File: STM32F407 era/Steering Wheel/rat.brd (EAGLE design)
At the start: 99.2 x 116.2 mm, 103 parts, among them IC3 PCA82C250T, Q1 12 MHz

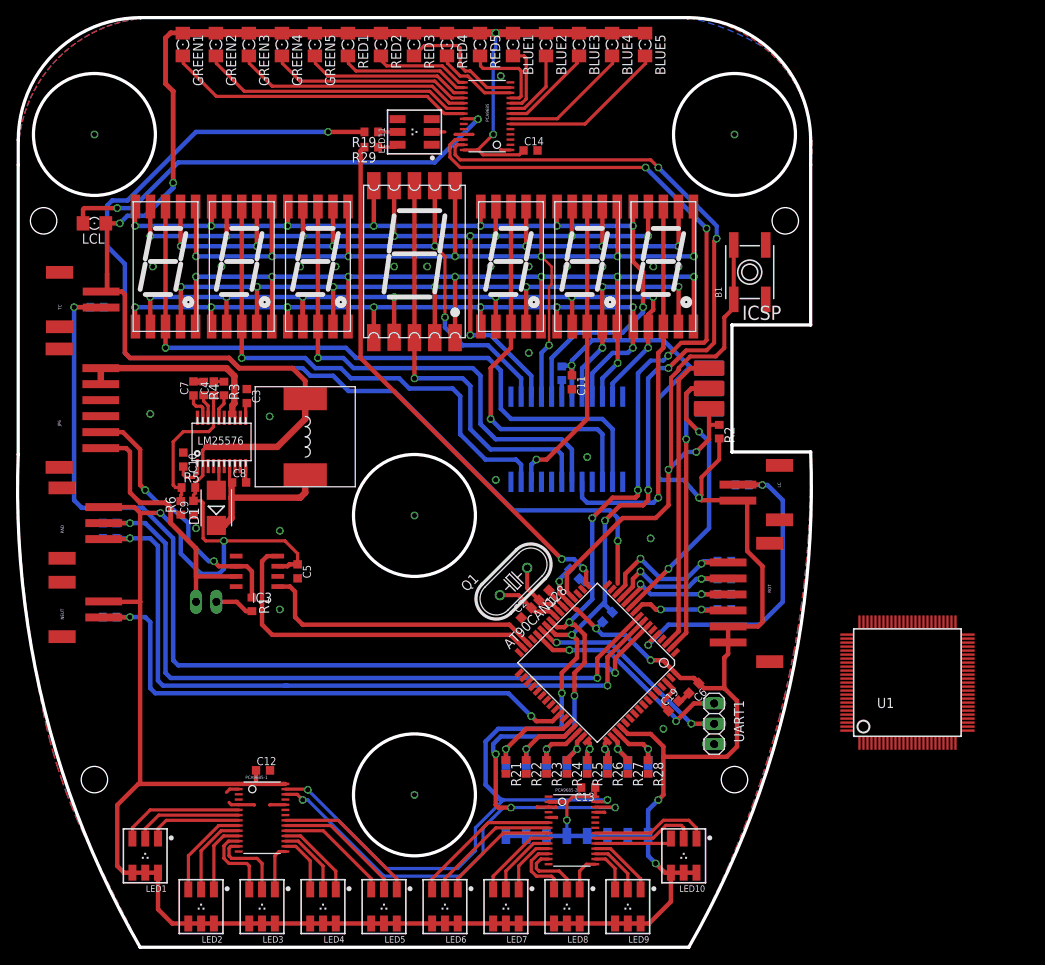
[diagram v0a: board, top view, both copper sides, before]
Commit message: added debounce handlers to critical buttons
Added MAX6817 debounce switches to the critical switches, and added the
acording datasheet
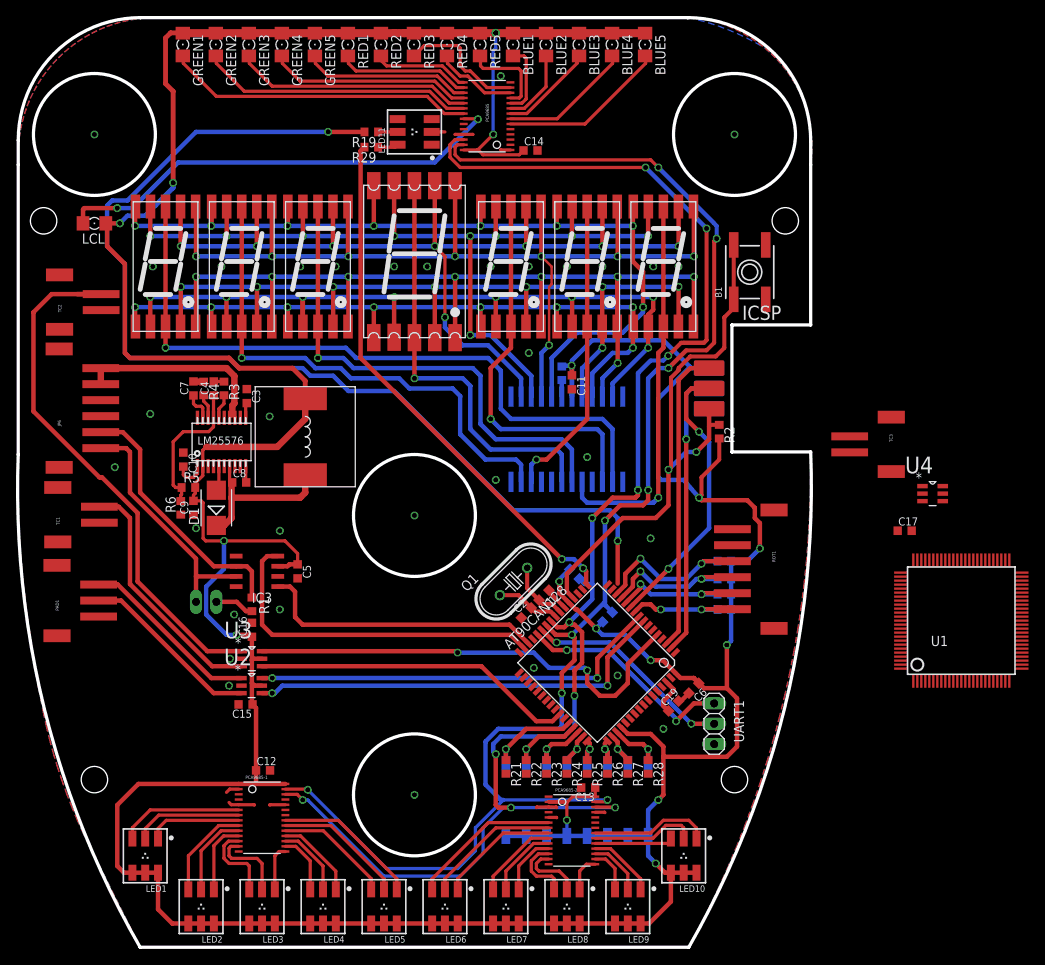
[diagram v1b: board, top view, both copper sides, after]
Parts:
- removed LC, NEUT, TC: (no value), unicorn_v2:S2B-PH
- removed PAD: (no value), unicorn_v2:S3B-PH
- removed R10, R12, R7, R8, R9: 10k, rcl:R0603
- removed ROT: M06, unicorn_v2:S6B_PH
- added C15, C16, C17: 100nF, rcl:C0603K
- added PAD1: (no value), unicorn_v2:S3B-PH
- added ROT1: M06, unicorn_v2:S6B_PH
- added TC1: NEUT, unicorn_v2:S2B-PH
- added TC2: LC, unicorn_v2:S2B-PH
- added TC3: tc, unicorn_v2:S2B-PH
- added U2, U3, U4: MAX6817EUT+T, Maxim_By_element14_Batch_1:SOT95P280X145-6N
- moved U1 10.3 mm to (290.0, 9.08)
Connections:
- new net N$85: TC1.2, U3.3
- new net N$86: PAD1.3, U2.1
- new net N$87: PAD1.2, U2.3
- new net N$88: TC2.2, U3.1
- new net N$90: TC3.2, U4.1
- net +5V: now also C15.1, C16.1, C17.1, R13.1, R14.1, R15.1, R16.1, U2.5, U3.5, U4.5; no longer LC.2, NEUT.2, PAD.3, ROT.5, ROT.6, TC.2
- net GND: now also C15.2, C16.2, C17.2, PAD1.1, ROT1.1, ROT1.2, TC1.1, TC2.1, TC3.1, U2.2, U3.2, U4.2; no longer R10.1, R12.1, R13.1, R14.1, R15.1, R16.1, R7.1, R8.1, R9.1
- net LC: now also U3.6; no longer LC.1, R9.2
- net NEUTRAL: now also U3.4; no longer NEUT.1, R8.2
- net PADDOWN: now also U2.4; no longer PAD.1, R10.2
- net PADUP: now also U2.6; no longer PAD.2, R12.2
- net ROTSW1: now also ROT1.6; no longer ROT.4
- net ROTSW2: now also ROT1.5; no longer ROT.3
- net ROTSW3: now also ROT1.4; no longer ROT.2
- net ROTSW4: now also ROT1.3; no longer ROT.1
- net TCTEMPOFF: now also U4.4; no longer R7.2, TC.1
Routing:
- net TCTEMPOFF: track 126.0 -> 0.00 mm, vias 2 -> 0
- net N$88: track 0.00 -> 68.3 mm
- net PADUP: track 90.8 -> 51.8 mm
- net PADDOWN: track 92.2 -> 53.6 mm
- net N$85: track 0.00 -> 30.9 mm
- net NEUTRAL: track 69.4 -> 40.5 mm, vias 2 -> 0
- net +5V: track 621.8 -> 593.1 mm, vias 15 -> 17
- net N$86: track 0.00 -> 22.7 mm
- net N$87: track 0.00 -> 22.7 mm
- net LC: track 41.7 -> 57.2 mm
- net CANJUMP1: track 32.9 -> 31.0 mm
- net ROTSW4: track 20.6 -> 21.5 mm
- net ROTSW1: track 14.4 -> 15.1 mm
- net ROTSW2: track 16.6 -> 17.3 mm
- net ROTSW3: track 18.5 -> 19.2 mm
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
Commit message: Redrawn the V2 of steering wheel to use ARM
Steering wheel V2 has been redrawn to use STM32F407 instead of the old
AT90CAN128.
Needs to be proberly looked through for any errors and oversights
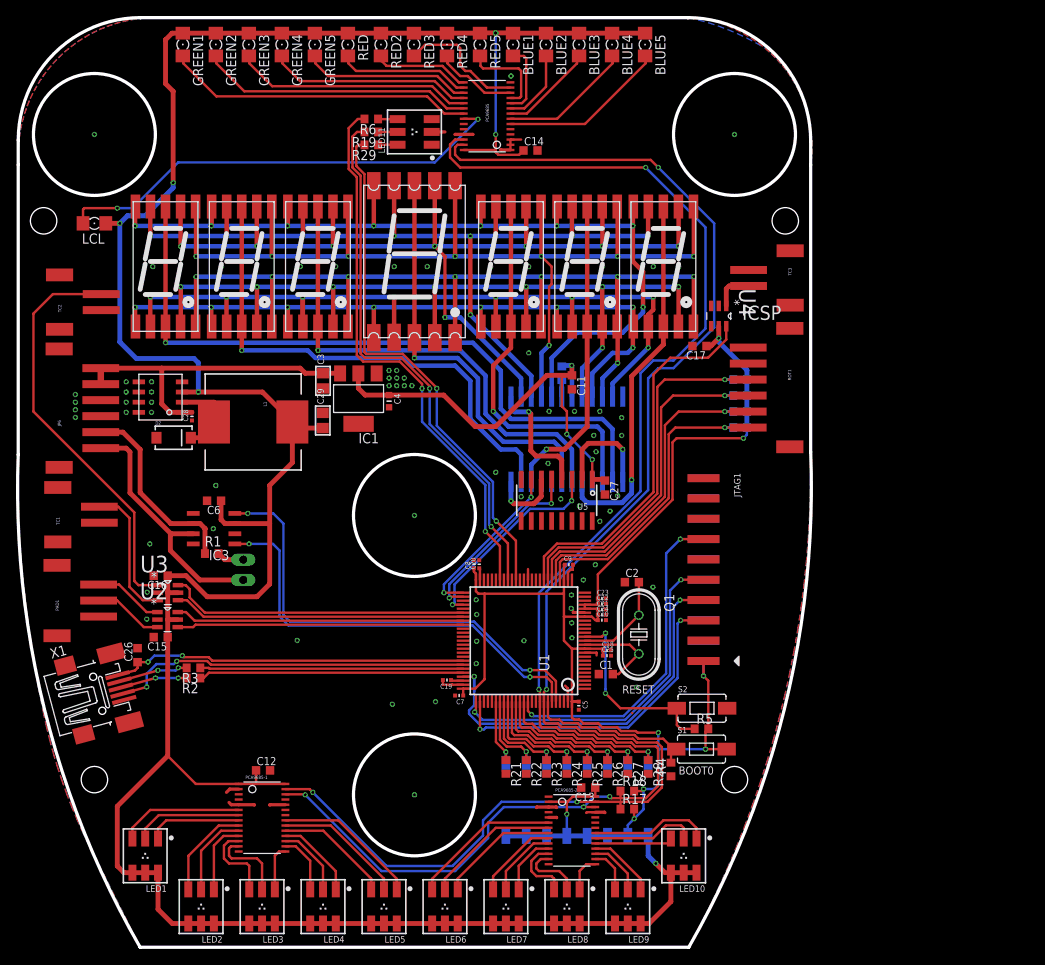
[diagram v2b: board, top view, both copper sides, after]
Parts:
- removed AT90CAN128: AT90CAN128, atmel:TQFP64
- removed B1: (no value), microbuilder:EVQ-Q2
- removed D1: SK54B R4, diode:SMB
- removed ICSP: ISP-HEADER, ISP-Header:ISP-HEADER
- removed U$1: LM25575, lm25576:LM25576
- removed U$9: INDUCTOR, unicorn_v2:INDUCTOR
- removed UART1: (no value), pinhead:1X03
- added C18, C21, C23, C28: 100n, microbuilder:_0402MP
- added C20: 2u2, microbuilder:_0402MP
- added C22, C24: 1u, microbuilder:_0402MP
- added C25: 4u7, microbuilder:_0402MP
- added C26: 4u7, rcl:C0603K
- added C27: 100nF, rcl:C0603K
- added C29: 10u, microbuilder:0805
- added D2: B340A-13-F, SparkFun-DiscreteSemi:SMA-DIODE
- added IC1: REG1117, burr-brown:SOT223
- added JTAG1: JTAG-ARMEDGE, microbuilder:MOLEX20_RIGHTANGLE
- added L1: MSS1038-473MLC 47u, SparkFun-Passives:CDRH125
- added S1, S2: (no value), SparkFun-Electromechanical:TACTILE-SWITCH-1101NE
- added U$10: AP1509, unicorn_v2:SOP-8L
- added U5: (no value), microbuilder:SOIC16
- added X1: MINI-USB-SCHIELD-32005-201, con-cypressindustries:32005-201
- BLUE1, BLUE2, BLUE3, BLUE4, BLUE5: value GREEN -> BLUE
- C10: value 0.01uf -> 100n; device rcl:C0603K -> microbuilder:_0402MP
- C19: value 100nF -> 2u2; device rcl:C0603K -> microbuilder:_0402MP
- C3: value 0.1uf -> 10u; device rcl:C0603K -> microbuilder:0805
- C4: value 0.01uf -> 22u; device rcl:C0603K -> microbuilder:_0603MP
- C5: value 100nF -> 100n; device rcl:C0603K -> microbuilder:_0402MP
- C7: value 47pf -> 100n; device rcl:C0603K -> microbuilder:_0402MP
- C8: value 0.022uf -> 100n; device rcl:C0603K -> microbuilder:_0402MP
- C9: value 140uf -> 100n; device rcl:C0603K -> microbuilder:_0402MP
- Q1: value 12 MHz -> 8 MHz
- R2: value (none) -> 22
- R3: value 49.9k -> 22
- R4: value 3.57k -> 500
- R5: value 15k -> 500
- R6: value 4.9k -> 220
- RED, RED2, RED3, RED4, RED5: value GREEN -> RED
- moved R4 75.4 mm to (253.7, -9.53), turned to 90 degrees
- moved R2 72.6 mm to (194.0, 1.91), turned to 180 degrees
- moved R5 70.9 mm to (257.5, -4.45)
- moved C6 64.4 mm to (196.6, 24.1), turned to 180 degrees
- moved C10 56.0 mm to (245.0, 9.14), turned to 0 degrees
- moved U1 54.7 mm to (235.3, 6.57), turned to 90 degrees
- moved R6 54.1 mm to (216.2, 71.8), turned to 180 degrees
- moved C7 50.8 mm to (227.2, -0.29), turned to 180 degrees
- moved C9 47.5 mm to (240.9, 16.1), turned to 0 degrees
- moved C5 39.0 mm to (242.2, -1.56)
- moved R3 35.1 mm to (194.0, 3.17), turned to 180 degrees
- moved U4 34.7 mm to (259.7, 47.1), turned to 270 degrees
- moved C17 34.5 mm to (257.2, 43.4), turned to 180 degrees
- moved C8 31.1 mm to (229.0, 16.1), turned to 90 degrees
- moved C19 28.5 mm to (225.7, 1.65), turned to 180 degrees
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- renumbered RED1 to RED
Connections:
- removed net +5V: 8-BIT-DIP.1, 8-BIT-DIP.2, 8-BIT-DIP.3, 8-BIT-DIP.4, 8-BIT-DIP.5, 8-BIT-DIP.6, 8-BIT-DIP.7, 8-BIT-DIP.8, AT90CAN128.21, AT90CAN128.52, AT90CAN128.64, BLUE1.A, BLUE2.A, BLUE3.A, BLUE4.A, BLUE5.A, C11.1, C12.1, C13.1, C14.1, C15.1, C16.1, C17.1, C5.1, C6.1, C9.2, GREEN1.A, GREEN2.A, GREEN3.A, GREEN4.A, GREEN5.A, IC3.3, ICSP.VDD, LCL.A, LED1.4, LED1.5, LED1.6, LED10.4, LED10.5, LED10.6, LED2.4, LED2.5, LED2.6, LED3.4, LED3.5, LED3.6, LED4.4, LED4.5, LED4.6, LED5.4, LED5.5, LED5.6, LED6.4, LED6.5, LED6.6, LED7.4, LED7.5, LED7.6, LED8.4, LED8.5, LED8.6, LED9.4, LED9.5, LED9.6, MAX7221.VCC, PCA9685-1.1, PCA9685-1.28, PCA9685-2.2, PCA9685-2.28, PCA9685.28, R11.1, R13.1, R14.1, R15.1, R16.1, R17.2, R18.2, R2.2, R5.2, RED.A, RED2.A, RED3.A, RED4.A, RED5.A, U$1.OUT, U$9.P$1, U2.5, U3.5, U4.5
- removed net MISO/TXD0: AT90CAN128.3, ICSP.MISO
- removed net MOSI/RXD0: AT90CAN128.2, ICSP.MOSI
- removed net N$29 (its old number): R3.2, U$1.COMP
- removed net N$32 (its old number): C8.2, U$1.BST
- removed net N$47: C10.2, U$1.SS
- removed net N$79: D1.A, U$1.IS
- removed net NEUTRAL: AT90CAN128.42, U3.4
- removed net PE: UART1.3
- removed net RXCAN: AT90CAN128.31, IC3.4
- removed net RXD1: AT90CAN128.27, UART1.2
- removed net SCK: AT90CAN128.11, ICSP.SCK
- removed net TXCAN: AT90CAN128.30, IC3.1
- removed net TXD1: AT90CAN128.28, UART1.1
- removed net VCC: JP6.5, JP6.6, U$1.VIN, U$1.VIN2
- removed net VDD: U1.100, U1.11, U1.19, U1.28, U1.50, U1.75
- removed net VDDA: U1.22
- removed net VSS: U1.10, U1.27, U1.74, U1.99
- removed net VSSA: U1.20
- new net 12V: C28.2, C3.2, IC1.3, JP6.5, JP6.6, U$10.P$1
- new net 3.3V: 8-BIT-DIP.1, 8-BIT-DIP.2, 8-BIT-DIP.3, 8-BIT-DIP.4, 8-BIT-DIP.5, 8-BIT-DIP.6, 8-BIT-DIP.7, 8-BIT-DIP.8, BLUE1.A, BLUE2.A, BLUE3.A, BLUE4.A, BLUE5.A, C10.1, C12.1, C13.1, C14.1, C15.1, C16.1, C17.1, C18.1, C21.1, C22.1, C23.1, C24.1, C25.1, C29.1, C5.1, C6.1, C7.1, C8.1, C9.1, GREEN1.A, GREEN2.A, GREEN3.A, GREEN4.A, GREEN5.A, IC3.3, JTAG1.1, JTAG1.2, L1.1, LCL.A, LED1.4, LED1.5, LED1.6, LED10.4, LED10.5, LED10.6, LED2.4, LED2.5, LED2.6, LED3.4, LED3.5, LED3.6, LED4.4, LED4.5, LED4.6, LED5.4, LED5.5, LED5.6, LED6.4, LED6.5, LED6.6, LED7.4, LED7.5, LED7.6, LED8.4, LED8.5, LED8.6, LED9.4, LED9.5, LED9.6, PCA9685-1.1, PCA9685-1.28, PCA9685-2.2, PCA9685-2.28, PCA9685.28, R13.1, R14.1, R15.1, R16.1, R17.2, R18.2, R5.2, RED.A, RED2.A, RED3.A, RED4.A, RED5.A, S1.P$2, U$10.P$3, U1.100, U1.11, U1.19, U1.21, U1.22, U1.28, U1.50, U1.75, U2.5, U3.5, U4.5
- new net 5.0V: C11.1, C27.1, C4.1, IC1.2, MAX7221.VCC, R11.1, U5.1
- new net CAN_RX: IC3.1, U1.95
- new net CAN_TX: IC3.4, U1.96
- new net JTAG-TCK: JTAG1.9, U1.76
- new net JTAG-TDI: JTAG1.5, U1.77
- new net JTAG-TDO: JTAG1.13, U1.89
- new net JTAG-TMS: JTAG1.7, U1.72
- new net NEUT: U1.57, U1.64, U3.4
- new net SLRED: R6.2, U1.44
- new net SPI-LOAD: U1.51, U5.7
- new net SPI-MISO: U1.53
- new net SPI-MOSI: U1.54, U5.3
- new net SPI-SCK: U1.52, U5.5
- new net USB_DM: R3.1, U1.70
- new net USB_DP: R2.1, U1.71
- new net USB_ID: U1.69, X1.4
- new net USB_VBUS: C26.1, U1.68, X1.1
- net DIP1: now also U1.81; no longer AT90CAN128.44
- net DIP2: now also U1.82; no longer AT90CAN128.45
- net DIP3: now also U1.83; no longer AT90CAN128.46
- net DIP4: now also U1.84; no longer AT90CAN128.47
- net DIP5: now also U1.85; no longer AT90CAN128.48
- net DIP6: now also U1.86; no longer AT90CAN128.49
- net DIP7: now also U1.87; no longer AT90CAN128.50
- net DIP8: now also U1.88; no longer AT90CAN128.51
- net GND: now also C10.2, C18.2, C20.2, C21.2, C22.2, C23.2, C24.2, C25.2, C26.2, C27.2, C28.1, C29.2, C4.2, C8.2, C9.2, D2.A, IC1.1, JTAG1.10, JTAG1.12, JTAG1.14, JTAG1.16, JTAG1.18, JTAG1.20, JTAG1.3, JTAG1.4, JTAG1.6, JTAG1.8, S2.P$2, U$10.P$4, U$10.P$5, U$10.P$6, U$10.P$7, U$10.P$8, U1.10, U1.20, U1.27, U1.37, U1.74, U1.99, U5.8, X1.5, X1.M1, X1.M2, X1.M3, X1.M4; no longer AT90CAN128.22, AT90CAN128.53, AT90CAN128.63, B1.A, B1.A', C10.1, C9.1, ICSP.GND, R6.1, U$1.AGND
- net LC: now also U1.56, U1.63; no longer AT90CAN128.5
- net N$1: now also U1.13; no longer AT90CAN128.24
- net N$10: now also U1.73; no longer AT90CAN128.62
- net N$2: now also U1.12; no longer AT90CAN128.23
- net N$24: now also C20.1, U1.49; no longer C4.1, R5.1, R6.2, U$1.FB
- net N$26: now also R2.2, X1.3; no longer C3.2, U$1.VCC
- net N$28: now also R3.2, X1.2; no longer C4.2, R3.1
- net N$30: now also S1.P$1, U1.94; no longer U$1.RT
- net N$31: now also R5.1, S2.P$1, U1.14; no longer C7.1, U$1.RAMP
- net N$33: now also LED11.4, R6.1; no longer C8.1, D1.C, U$1.SW, U$9.P$2
- net N$4: now also U5.4
- net N$46: now also D2.C, L1.2, U$10.P$2; no longer AT90CAN128.6
- net N$5: now also U5.6
- net N$7: now also U5.2
- net PADDOWN: now also U1.59, U1.66; no longer AT90CAN128.8
- net PADUP: now also U1.58, U1.65; no longer AT90CAN128.9
- net RESET: now also JTAG1.15; no longer AT90CAN128.20, B1.B, B1.B', ICSP.RST, R2.1
- net ROTSW1: now also U1.29; no longer AT90CAN128.10
- net ROTSW2: now also U1.30; no longer AT90CAN128.12
- net ROTSW3: now also U1.31; no longer AT90CAN128.13
- net ROTSW4: now also U1.32; no longer AT90CAN128.14
- net SCL: now also U1.92; no longer AT90CAN128.25
- net SDA: now also U1.93; no longer AT90CAN128.26
- net SLBLUE: now also U1.40; no longer AT90CAN128.17
- net SLGREEN: now also U1.42; no longer AT90CAN128.15
- net TCTEMPOFF: now also U1.33, U4.6; no longer AT90CAN128.7, U4.4
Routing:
- net +5V: track 593.1 -> 0.00 mm, vias 17 -> 0
- net 3.3V: track 0.00 -> 551.3 mm, vias 0 -> 15
- net SLRED: track 0.00 -> 69.4 mm, vias 0 -> 2
- net RESET: track 69.4 -> 0.00 mm, vias 2 -> 0
- net SLGREEN: track 133.7 -> 67.9 mm
- net CAN_TX: track 0.00 -> 58.1 mm, vias 0 -> 2
- net 5.0V: track 0.00 -> 56.2 mm, vias 0 -> 3
- net CAN_RX: track 0.00 -> 54.0 mm, vias 0 -> 2
- net JTAG-TMS: track 0.00 -> 49.6 mm, vias 0 -> 2
- net TCTEMPOFF: track 0.00 -> 47.2 mm
- net USB_ID: track 0.00 -> 45.2 mm, vias 0 -> 2
- net USB_VBUS: track 0.00 -> 44.7 mm, vias 0 -> 2
- net RXCAN: track 44.1 -> 0.00 mm
- net JTAG-TCK: track 0.00 -> 43.8 mm, vias 0 -> 2
- net JTAG-TDO: track 0.00 -> 41.4 mm, vias 0 -> 2
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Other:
- outline, holes or cut-outs redrawn
- board text added: "BOOT0"
- board text added: "RESET"

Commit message: added cutout for jtag header.
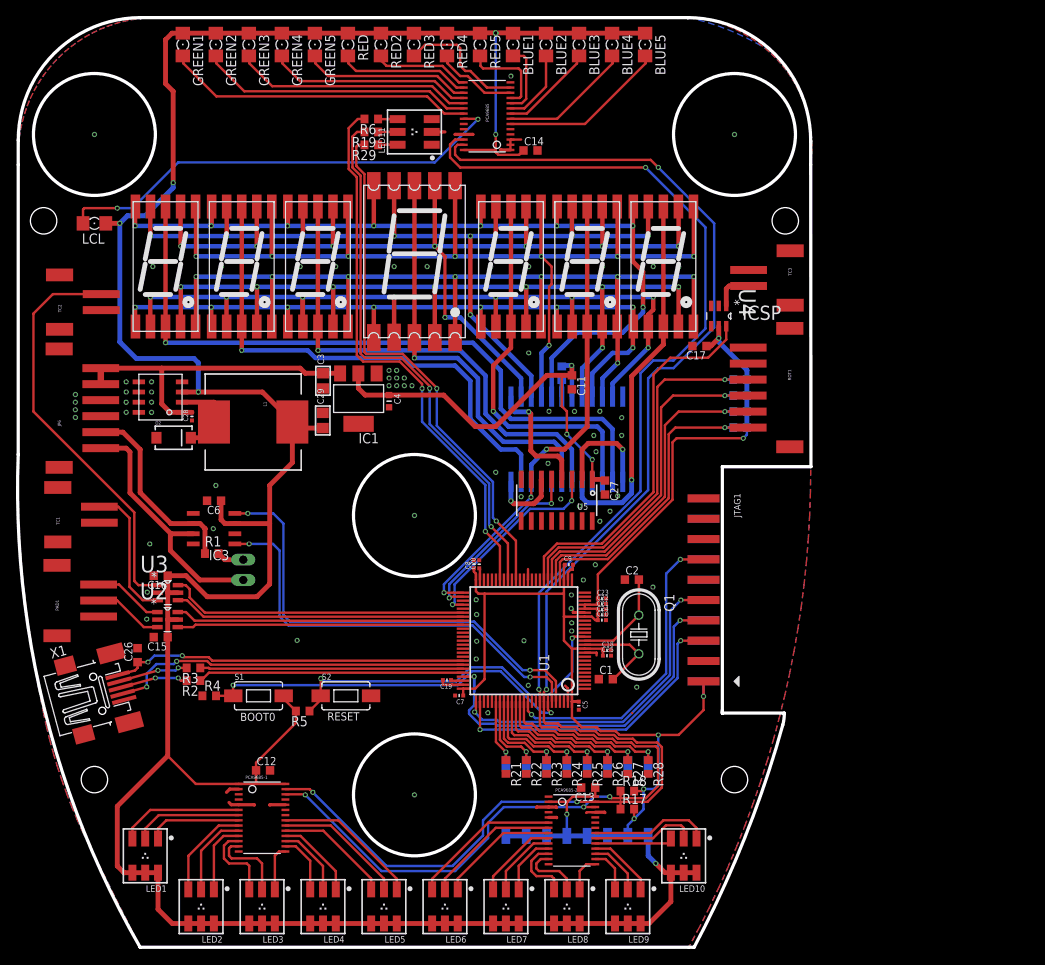
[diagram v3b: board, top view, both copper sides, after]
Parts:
- moved R4 58.5 mm to (196.0, -0.32), turned to 0 degrees
- moved S1 55.8 mm to (202.1, -0.32)
- moved R5 49.9 mm to (207.6, -2.22), turned to 180 degrees
- moved S2 44.5 mm to (213.0, -0.32)
- moved JTAG1 2.54 mm to (257.7, 12.9)
- moved C1 0.64 mm to (245.5, 1.76)
- moved C2 0.32 mm to (248.8, 14.2)
- moved R2 0.32 mm to (194.0, 1.59)
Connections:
- net LC: no longer U1.63
- net NEUT: no longer U1.64
- net PADDOWN: no longer U1.66
- net PADUP: no longer U1.65
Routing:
- net N$30: track 21.5 -> 47.7 mm, vias 0 -> 2
- net N$31: track 24.5 -> 45.9 mm
- net JTAG-TDI: track 41.1 -> 38.6 mm
- net 3.3V: track 551.3 -> 553.8 mm, vias 15 -> 14
- net JTAG-TCK: track 43.8 -> 41.5 mm
- net JTAG-TMS: track 49.6 -> 47.2 mm
- net JTAG-TDO: track 41.4 -> 39.0 mm
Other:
- outline, holes or cut-outs redrawn

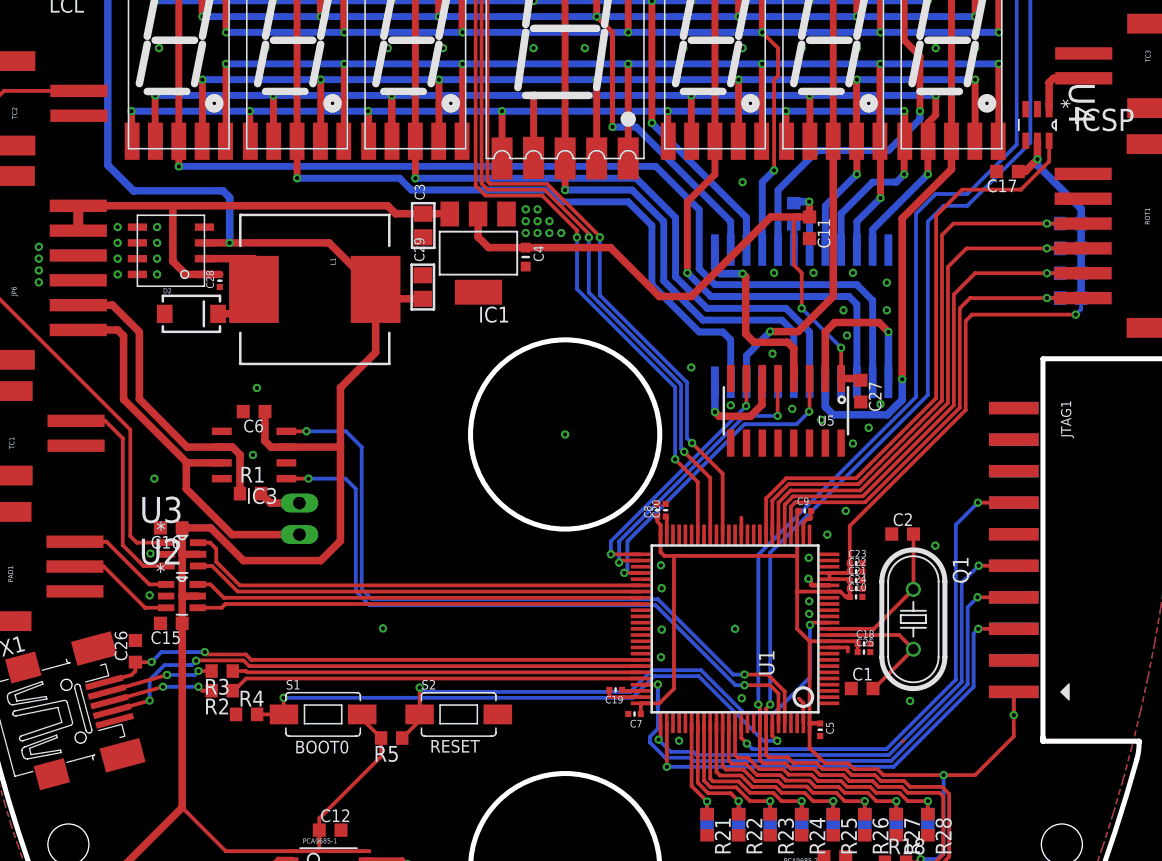
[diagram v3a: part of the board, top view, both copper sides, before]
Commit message: circuit changes, and added rasp pi hat footprint
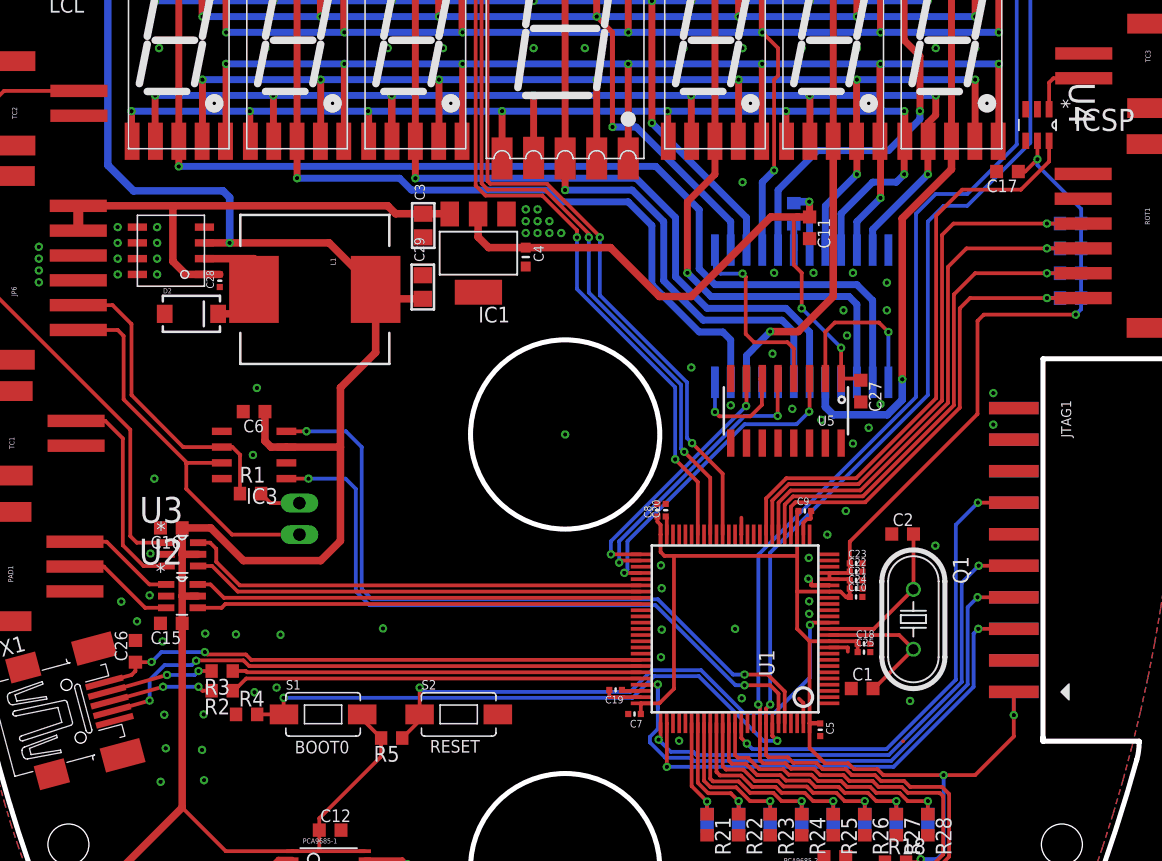
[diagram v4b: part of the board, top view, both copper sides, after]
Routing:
- net 3.3V: track 553.8 -> 553.2 mm
- net GND: vias 71 -> 87
